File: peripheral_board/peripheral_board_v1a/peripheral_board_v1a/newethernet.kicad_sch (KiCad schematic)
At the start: 85 parts, among them SW4 EVPAA602W, U6 AZ1117CH-1.2TRG1, U7 KSZ8795CLXIC, Y3 ABMM-25.000MHZ-B2-T

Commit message: PCB Update
Got all the parts on the board placed. Now just finishing the routing for each interconnection.
Trying to maintain a side to side/up to down but the board kinda follows it. For each plane  there is fill zones that will be for the chip that is on the top. Some of the traces are just being fed to where they need to go but the important EMI signals are being contained to their guidelines.
I will need to look at the lengths of the traces to make sure they are kept around the same length.

Will need to go over the board with some other eyes to make sure its ok.

I made sure the Wiznet traces are the same as SALAD.
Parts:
- removed C45, C46: 100nF, Capacitor_SMD:C_0402_1005Metric, symbol Device:C
- removed C47, C48: 10nF, Capacitor_SMD:C_0402_1005Metric, symbol Device:C
- removed D4, D5: LED, LED_SMD:LED_0603_1608Metric, symbol Device:LED
- removed R47, R48: 330, Resistor_SMD:R_0603_1608Metric, symbol Device:R_US
- renumbered C35 to C36, C36 to C37, C37 to C38, C38 to C39, C41 to C40, C49 to C41, C50 to C42, C51 to C43, C55 to C44, C52 to C45, C53 to C46, C54 to C47, C34 to C48, C39 to C49, C40 to C50, C56 to C51, C42 to C52, C57 to C53, C43 to C54, C44 to C55, C58 to C56, FB5 to FB3, FB3 to FB4, FB6 to FB5, FB4 to FB6, R39 to R34, R40 to R35, R35 to R36, R36 to R37, R37 to R38, R38 to R39, R41 to R40, R42 to R41, R43 to R42, R44 to R43, R45 to R44, R46 to R45, R49 to R48, U7 to U6, U6 to U7
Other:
- note removed: "INT"
- note removed: "PME"

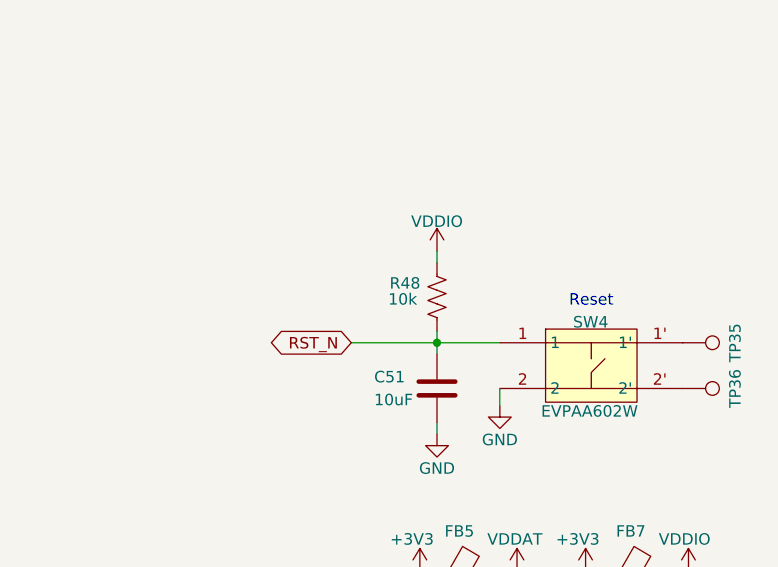
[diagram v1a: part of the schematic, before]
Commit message: PCB almost done
Finished the routing except for the power board connector. Will be looking into adding in a Power path controller or similar. Want to add in via stitching for the DP signals. Should be just about done it would be more of just doing some change/improvements.
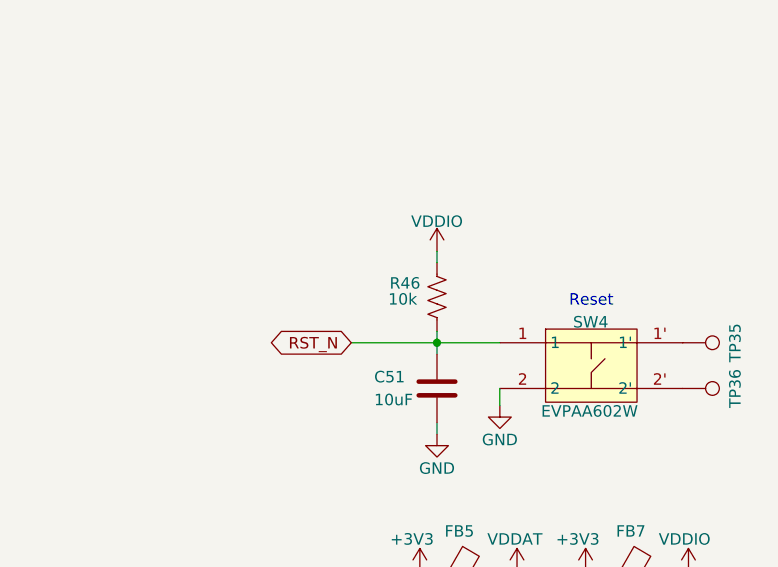
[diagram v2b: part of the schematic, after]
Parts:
- SW4: footprint easyeda2kicad:KEY-TH_4P-L3.5-W4.9-P2.80-LS4.3 -> SCALES:KEY-TH_4P-L3.5-W4.9-P2.80-LS4.3
- renumbered R48 to R46

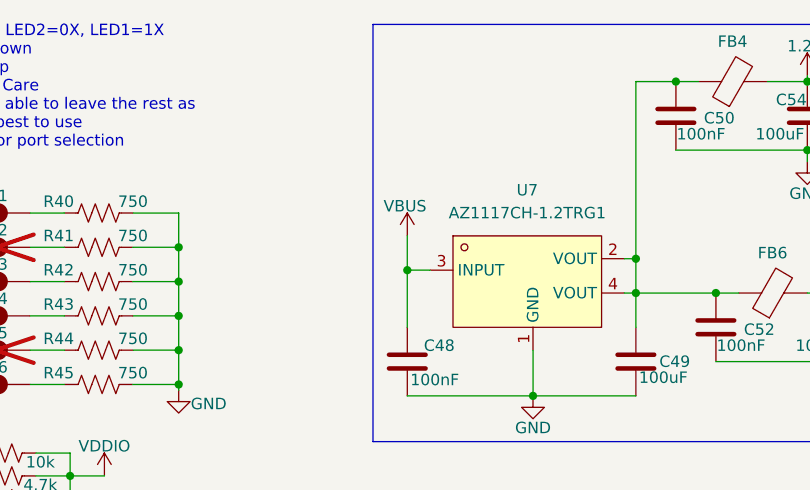
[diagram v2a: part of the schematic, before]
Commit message: PCB should be done
Finished the PCB just needs a review and then the part selection should be easy.
Added in stitching Vias.
Added in a Power controller for the two power sources of the USB or the external power board.
Removed the microSD card reader and added in XTSD which is just onboard NAND. It is around 1 gigabyte which should be enough space for any and all programs we are running.
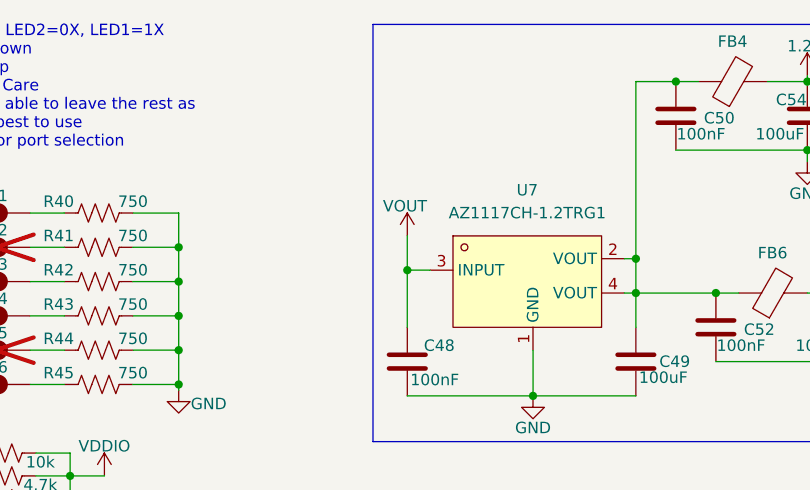
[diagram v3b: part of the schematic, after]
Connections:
- net VBUS renamed VOUT
